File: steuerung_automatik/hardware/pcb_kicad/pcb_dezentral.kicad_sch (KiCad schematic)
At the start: 37 parts, among them J1 USB_C_Receptacle_USB2.0, SW1 SW_MEC_5E, SW2 SW_MEC_5E, U1 RP2040, U2 W25Q128JVS, U3 AMS1117-3.3, Y1 Crystal_GND24_Small

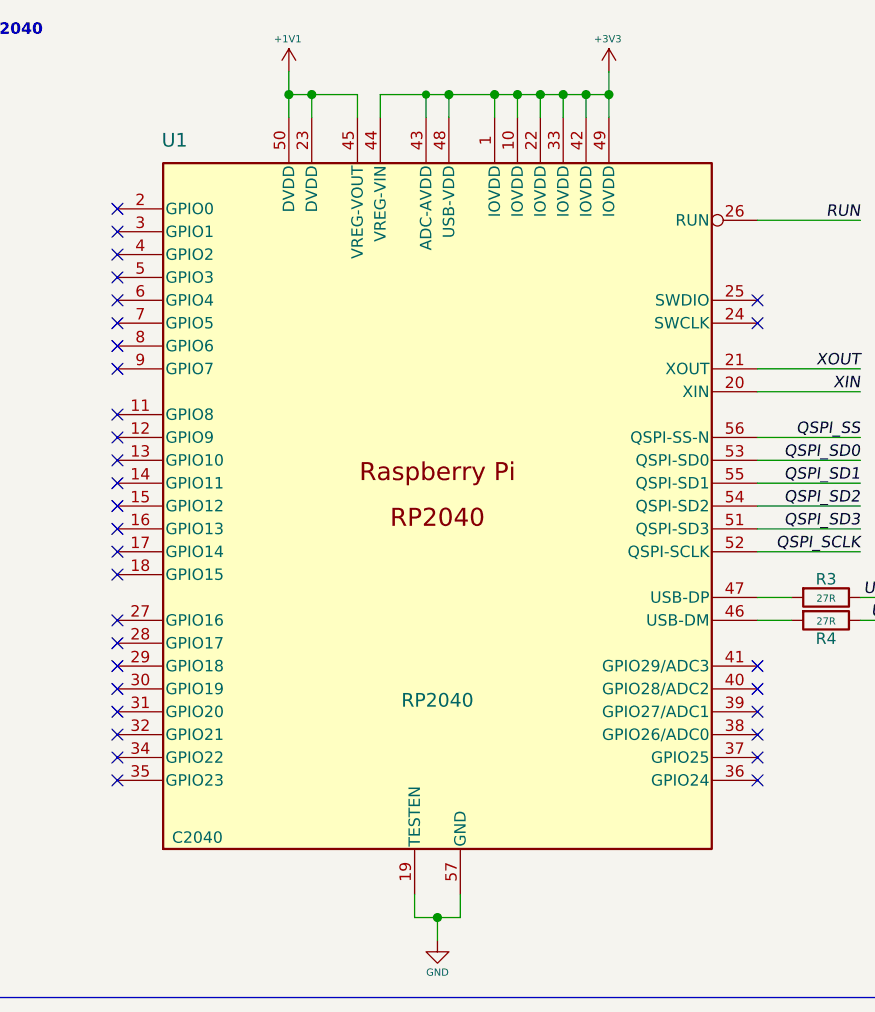
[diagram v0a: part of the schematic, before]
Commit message: Renamed to pcb_dezentral
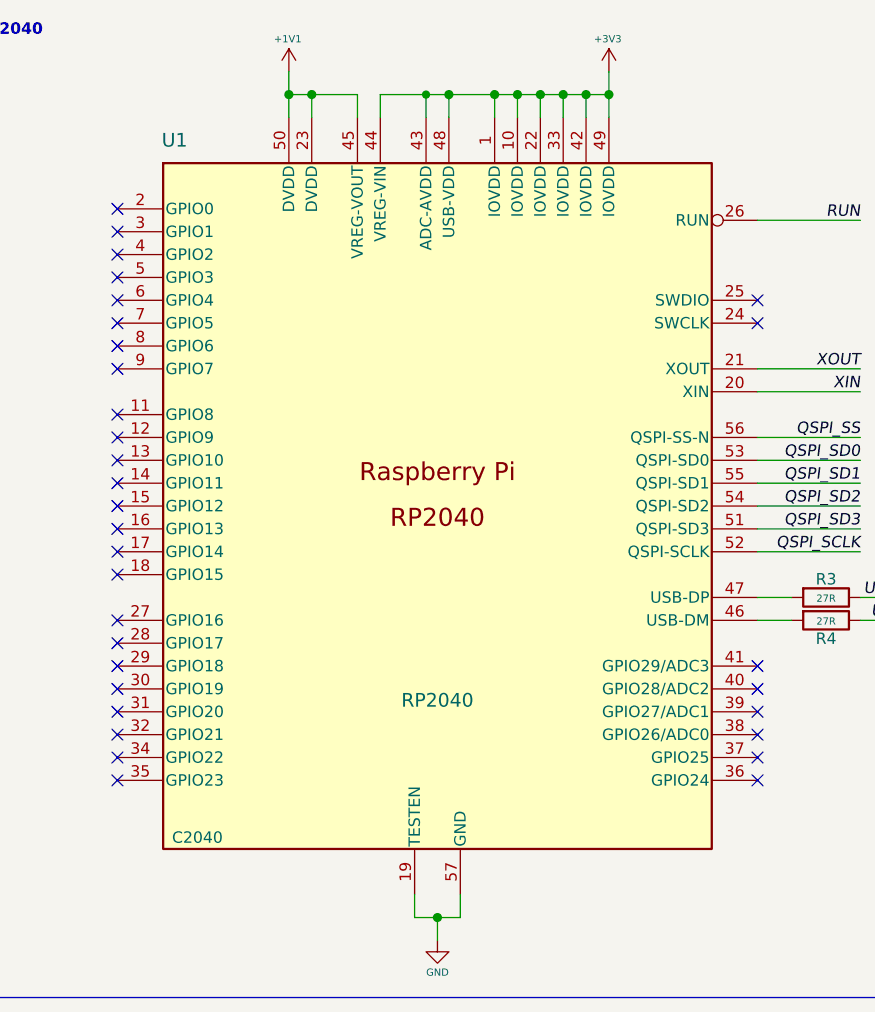
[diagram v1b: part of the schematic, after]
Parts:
- U1: footprint Package_DFN_QFN:QFN-56-1EP_7x7mm_P0.4mm_EP5.6x5.6mm -> 00_project_library:RP2040-QFN-56
- U3: footprint Package_TO_SOT_SMD:SOT-223-3_TabPin2 -> 00_project_library:SOT-223-3_TabPin2
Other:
- company: Salami Brother -> www.positron.ch
- title: 2023_filament_dryer -> Heizung Pünterswis - pcb_zentral

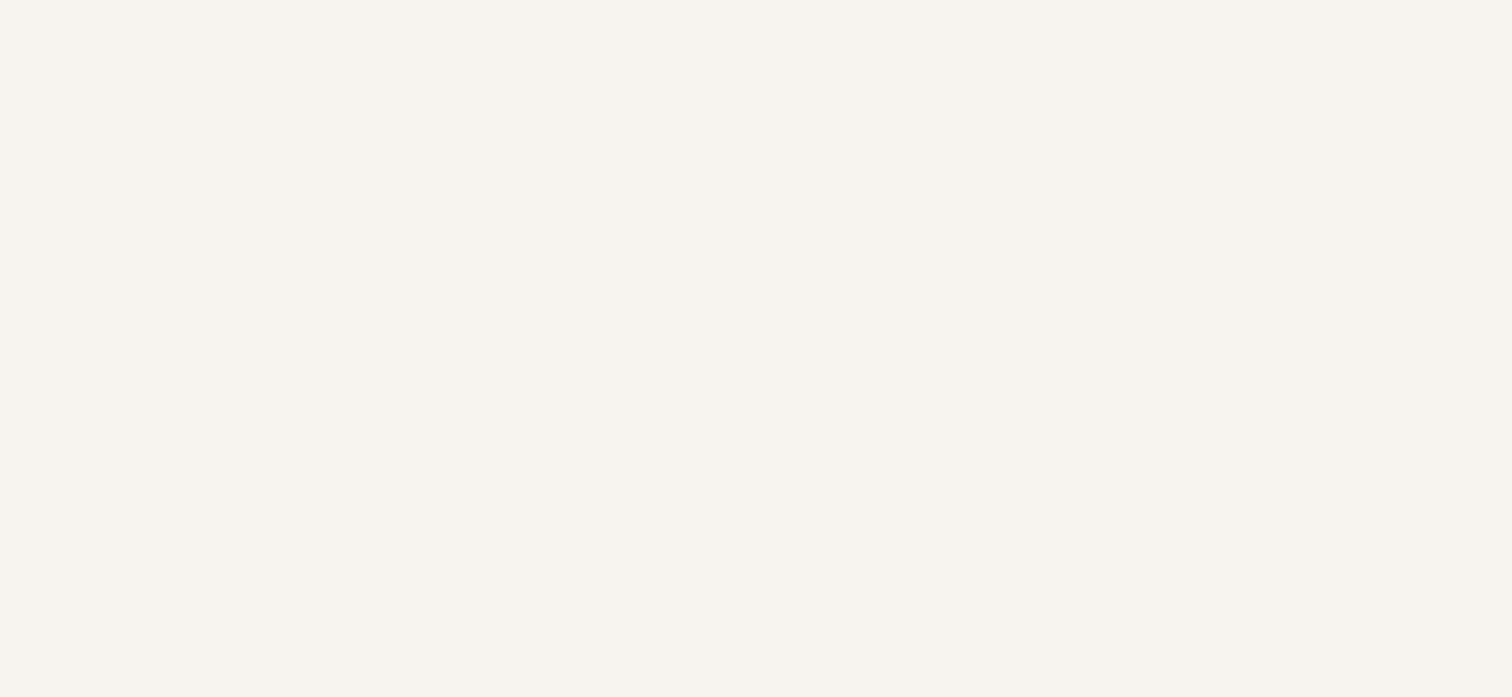
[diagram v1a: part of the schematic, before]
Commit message: Added footprints
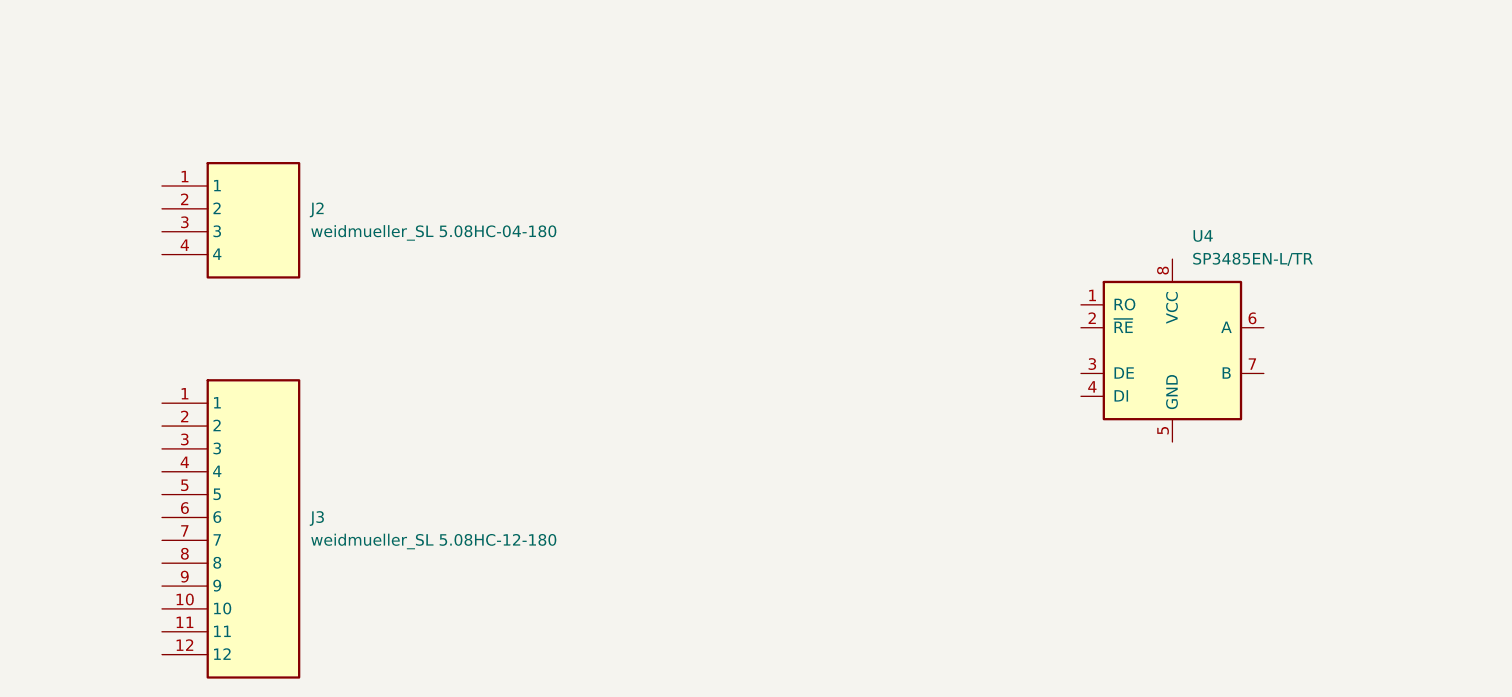
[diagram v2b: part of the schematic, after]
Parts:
- added J2: weidmueller_SL 5.08HC-04-180, 00_project_library:weidmueller_SL 5.08HC-04-180, symbol 00_project_library:weidmueller_SL 5.08HC-04-180
- added J3: weidmueller_SL 5.08HC-12-180, 00_project_library:weidmueller_SL 5.08HC-12-180, symbol 00_project_library:weidmueller_SL 5.08HC-12-180
- added U4: SP3485EN-L/TR, Package_SO:SOIC-8_3.9x4.9mm_P1.27mm, symbol 00_project_library:modbus_SP3485EN
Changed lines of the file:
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@@
+    )
+  )
+  (symbol (lib_id "00_project_library:weidmueller_SL 5.08HC-04-180") (at 175.26 174.752 0) (unit 1)
+    (in_bom yes) (on_board yes) (dnp no) (fields_autoplaced)
+    (property "Reference" "J2" (at 191.77 177.292 0)
+      (effects (font (size 1.27 1.27)) (justify left))
+    )
+    (property "Value" "weidmueller_SL 5.08HC-04-180" (at 191.77 179.832 0)
+      (effects (font (size 1.27 1.27)) (justify left))
+    )
+    (property "Footprint" "00_project_library:weidmueller_SL 5.08HC-04-180" (at 191.77 269.672 0)
+      (effects (font (size 1.27 1.27)) (justify left top) hide)
+    )
+    (property "Datasheet" "http://catalog.weidmueller.com/createDatasheetForMobile.do?ordernumber=1146380000&scope1=1&scope2=1&localeId=en" (at 191.77 369.672 0)
+      (effects (font (size 1.27 1.27)) (justify left top) hide)
+    )
+    (property "Height" "12" (at 191.77 569.672 0)
+      (effects (font (size 1.27 1.27)) (justify left top) hide)
+    )
+    (property "Manufacturer_Name" "Weidmuller" (at 191.77 669.672 0)
+      (effects (font (size 1.27 1.27)) (justify left top) hide)
+    )
+    (property "Manufacturer_Part_Number" "1146380000" (at 191.77 769.672 0)
+      (effects (font (size 1.27 1.27)) (justify left top) hide)
+    )
+    (property "Mouser Part Number" "470-1146380000" (at 191.77 869.672 0)
+      (effects (font (size 1.27 1.27)) (justify left top) hide)
+    )
+    (property "Mouser Price/Stock" "https://www.mouser.co.uk/ProductDetail/Weidmuller/1146380000?qs=WJDKaGZ8K%252B5M5T7FYz8XlQ%3D%3D" (at 191.77 969.672 0)
+      (effects (font (size 1.27 1.27)) (justify left top) hide)
+    )
+    (property "Arrow Part Number" "" (at 191.77 1069.672 0)
+      (effects (font (size 1.27 1.27)) (justify left top) hide)
+    )
+    (property "Arrow Price/Stock" "" (at 191.77 1169.672 0)
+      (effects (font (size 1.27 1.27)) (justify left top) hide)
+    )
+    (pin "1")
+    (pin "2")
+    (pin "3")
+    (pin "4")
+    (instances
+      (project "pcb_dezentral"
+        (path "/35c47459-45a7-4753-acae-c8b47e7575e1"
+          (reference "J2") (unit 1)
+        )
+      )
     )
   )
@@
     )
   )
+  (symbol (lib_id "00_project_library:modbus_SP3485EN") (at 287.528 193.04 0) (unit 1)
+    (in_bom yes) (on_board yes) (dnp no) (fields_autoplaced)
+    (property "Reference" "U4" (at 289.7221 180.34 0)
+      (effects (font (size 1.27 1.27)) (justify left))
+    )
+    (property "Value" "SP3485EN-L/TR" (at 289.7221 182.88 0)
+      (effects (font (size 1.27 1.27)) (justify left))
+    )
+    (property "Footprint" "Package_SO:SOIC-8_3.9x4.9mm_P1.27mm" (at 314.198 201.93 0)
+      (effects (font (size 1.27 1.27) italic) hide)
+    )
+    (property "Datasheet" "http://www.icbase.com/pdf/SPX/SPX00480106.pdf" (at 287.528 193.04 0)
+      (effects (font (size 1.27 1.27)) hide)
+    )
+    (property "DatasheetJLC" " https://datasheet.lcsc.com/lcsc/2304140030_MaxLinear-SP3485EN-L-TR_C8963.pdf" (at 287.528 193.04 0)
+      (effects (font (size 1.27 1.27)) hide)
+    )
+    (property "JLC" "C8963" (at 287.528 193.04 0)
+      (effects (font (size 1.27 1.27)) hide)
+    )
+    (pin "1")
+    (pin "2")
+    (pin "3")
+    (pin "4")
+    (pin "5")
+    (pin "6")
+    (pin "7")
+    (pin "8")
+    (instances
+      (project "pcb_dezentral"
+        (path "/35c47459-45a7-4753-acae-c8b47e7575e1"
+          (reference "U4") (unit 1)
+        )
+      )
+    )
+  )
   (symbol (lib_id "00_project_library:C") (at 260.35 40.64 0) (unit 1)
     (in_bom yes) (on_board yes) (dnp no)
@@
         )
       )
+    )
+  )
+  (symbol (lib_id "00_project_library:weidmueller_SL 5.08HC-12-180") (at 175.26 198.882 0) (unit 1)
+    (in_bom yes) (on_board yes) (dnp no) (fields_autoplaced)
+    (property "Reference" "J3" (at 191.77 211.582 0)
+      (effects (font (size 1.27 1.27)) (justify left))
+    )
+    (property "Value" "weidmueller_SL 5.08HC-12-180" (at 191.77 214.122 0)
+      (effects (font (size 1.27 1.27)) (justify left))
+    )
+    (property "Footprint" "00_project_library:weidmueller_SL 5.08HC-12-180" (at 191.77 293.802 0)
+      (effects (font (size 1.27 1.27)) (justify left top) hide)
+    )
+    (property "Datasheet" "http://catalog.weidmueller.com/createDatasheetForMobile.do?ordernumber=1146570000&scope1=1&scope2=1&localeId=en" (at 191.77 393.802 0)
+      (effects (font (size 1.27 1.27)) (justify left top) hide)
+    )
+    (property "Height" "12" (at 191.77 593.802 0)
+      (effects (font (size 1.27 1.27)) (justify left top) hide)
+    )
+    (property "Manufacturer_Name" "Weidmuller" (at 191.77 693.802 0)
+      (effects (font (size 1.27 1.27)) (justify left top) hide)
+    )
+    (property "Manufacturer_Part_Number" "1146570000" (at 191.77 793.802 0)
+      (effects (font (size 1.27 1.27)) (justify left top) hide)
+    )
+    (property "Mouser Part Number" "470-1146570000" (at 191.77 893.802 0)
+      (effects (font (size 1.27 1.27)) (justify left top) hide)
+    )
+    (property "Mouser Price/Stock" "https://www.mouser.co.uk/ProductDetail/Weidmuller/1146570000?qs=WJDKaGZ8K%252B7cP7z9TJi1CA%3D%3D" (at 191.77 993.802 0)
+      (effects (font (size 1.27 1.27)) (justify left top) hide)
+    )
+    (property "Arrow Part Number" "" (at 191.77 1093.802 0)
+      (effects (font (size 1.27 1.27)) (justify left top) hide)
+    )
+    (property "Arrow Price/Stock" "" (at 191.77 1193.802 0)
+      (effects (font (size 1.27 1.27)) (justify left top) hide)
+    )
+    (pin "1")
+    (pin "10")
+    (pin "11")
+    (pin "12")
+    (pin "2")
+    (pin "3")
+    (pin "4")
+    (pin "5")
+    (pin "6")
+    (pin "7")
+    (pin "8")
+    (pin "9")
+    (instances
+      (project "pcb_dezentral"
+        (path "/35c47459-45a7-4753-acae-c8b47e7575e1"
+          (reference "J3") (unit 1)
+        )
+      )

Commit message: Nach Review
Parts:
- J102: renamed from J2; value weidmueller_SL 5.08HC-04-180 -> weidmueller_SL5.08HC-04-90; footprint 00_project_library:weidmueller_SL 5.08HC-04-180 -> 00_project_library:weidmueller_SL5.08HC-04-90; symbol 00_project_library:weidmueller_SL 5.08HC-04-180 -> 00_project_library:weidmueller_SL5.08HC-04-90; Height 12 -> 8.4; Manufacturer_Part_Number 1146380000 -> 1146770000; Mouser Part Number 470-1146380000 -> 470-1146770000; Mouser Price/Stock https://www.mouser.co.uk/ProductDetail/Weidmuller/114638000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 -> https://www.mouser.co.uk/ProductDetail/Weidmuller/114677000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
- J103: renamed from J3; value weidmueller_SL 5.08HC-12-180 -> weidmueller_SL5.08HC-12-90; footprint 00_project_library:weidmueller_SL 5.08HC-12-180 -> 00_project_library:weidmueller_SL5.08HC-12-90; symbol 00_project_library:weidmueller_SL 5.08HC-12-180 -> 00_project_library:weidmueller_SL5.08HC-12-90; Height 12 -> 8.4; JLC (none) -> C6186; Manufacturer_Part_Number 1146570000 -> 1146940000
- renumbered C1 to C101, C2 to C102, C3 to C103, C4 to C104, C5 to C105, C6 to C106, C7 to C107, C8 to C108, C9 to C109, C10 to C110, C11 to C111, C12 to C112, C13 to C113, C14 to C114, C15 to C115, C16 to C116, D1 to D101, H1 to H101, H2 to H102, H3 to H103, H4 to H104, J1 to J101, R1 to R101, R2 to R102, R3 to R103, R4 to R104, R5 to R105, R6 to R106, R7 to R107, R8 to R108, SW1 to SW101, SW2 to SW102, TP1 to TP101, U1 to U101, U2 to U102, U4 to U103, U3 to U104, Y1 to Y101

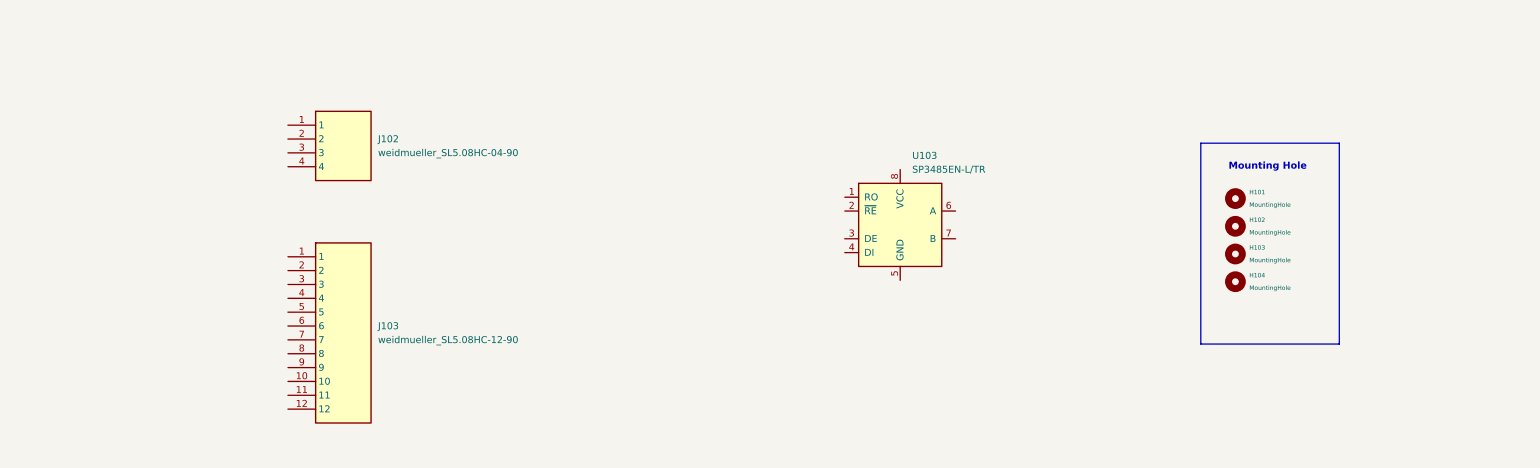
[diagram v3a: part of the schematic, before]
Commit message: Add weidmueller and din_rail_pcb_holder footprints
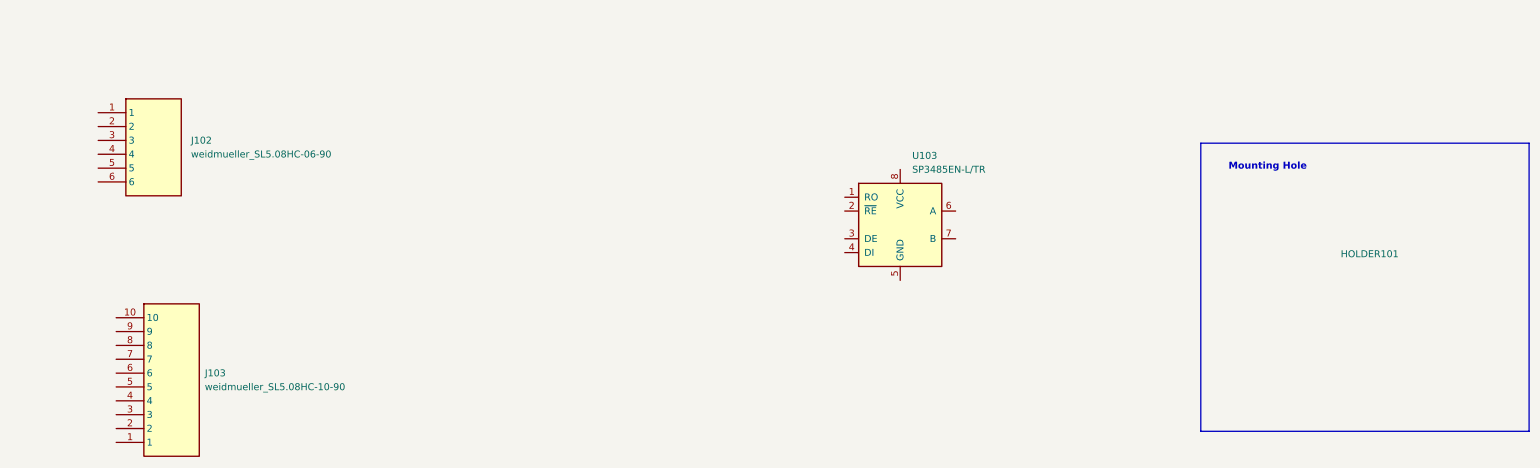
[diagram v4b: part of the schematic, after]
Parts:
- removed H101, H102, H103, H104: MountingHole, MountingHole:MountingHole_3.2mm_M3, symbol 00_project_library:MountingHole
- removed J102: weidmueller_SL5.08HC-04-90, 00_project_library:weidmueller_SL5.08HC-04-90, symbol 00_project_library:weidmueller_SL5.08HC-04-90
- removed J103: weidmueller_SL5.08HC-12-90, 00_project_library:weidmueller_SL5.08HC-12-90, symbol 00_project_library:weidmueller_SL5.08HC-12-90
- added HOLDER101: ~, 00_project_library:din_rail_pcb_holder, symbol 00_project_library:din_rail_pcb_holder
- added J102: weidmueller_SL5.08HC-06-90, 00_project_library:weidmueller_SL5.08HC-06-90, symbol 00_project_library:weidmueller_SL5.08HC-06-90
- added J103: weidmueller_SL5.08HC-10-90, 00_project_library:weidmueller_SL5.08HC-10-90, symbol 00_project_library:weidmueller_SL5.08HC-10-90
